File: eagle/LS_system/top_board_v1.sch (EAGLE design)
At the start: 18 parts, among them IC1 74HC595D, X1 MURDOCK_STACK

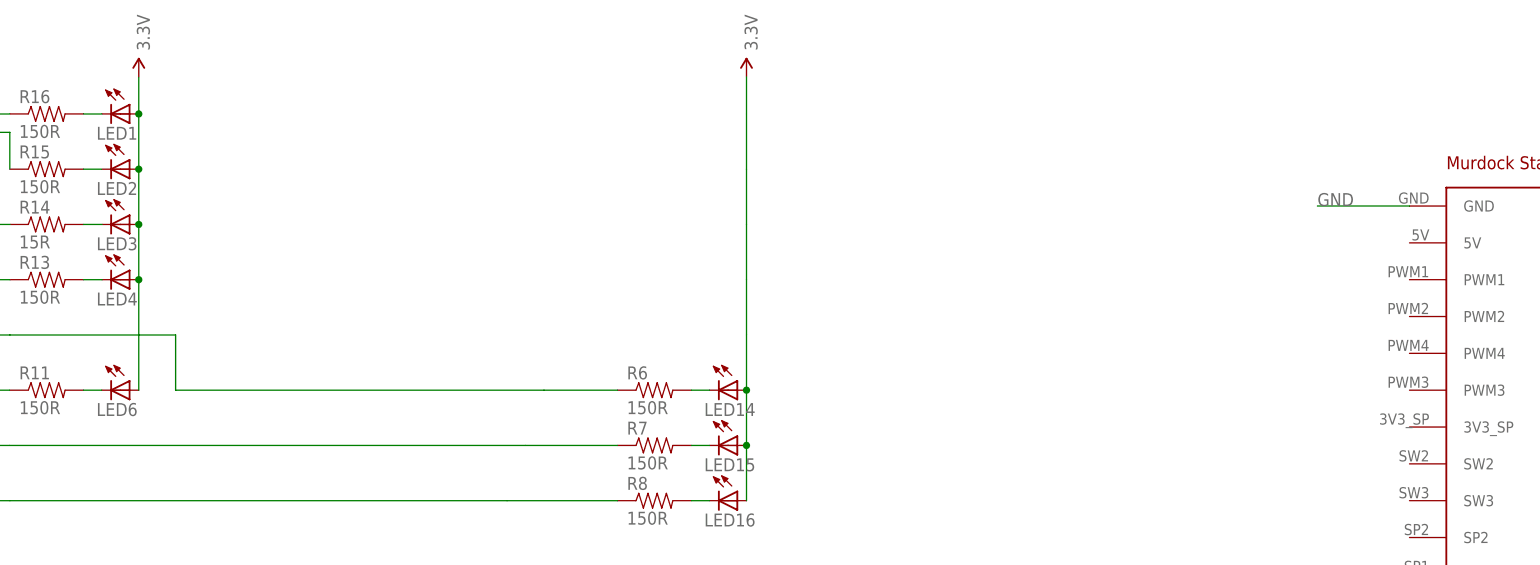
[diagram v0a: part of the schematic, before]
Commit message: conneced LEDs to switche 3v3
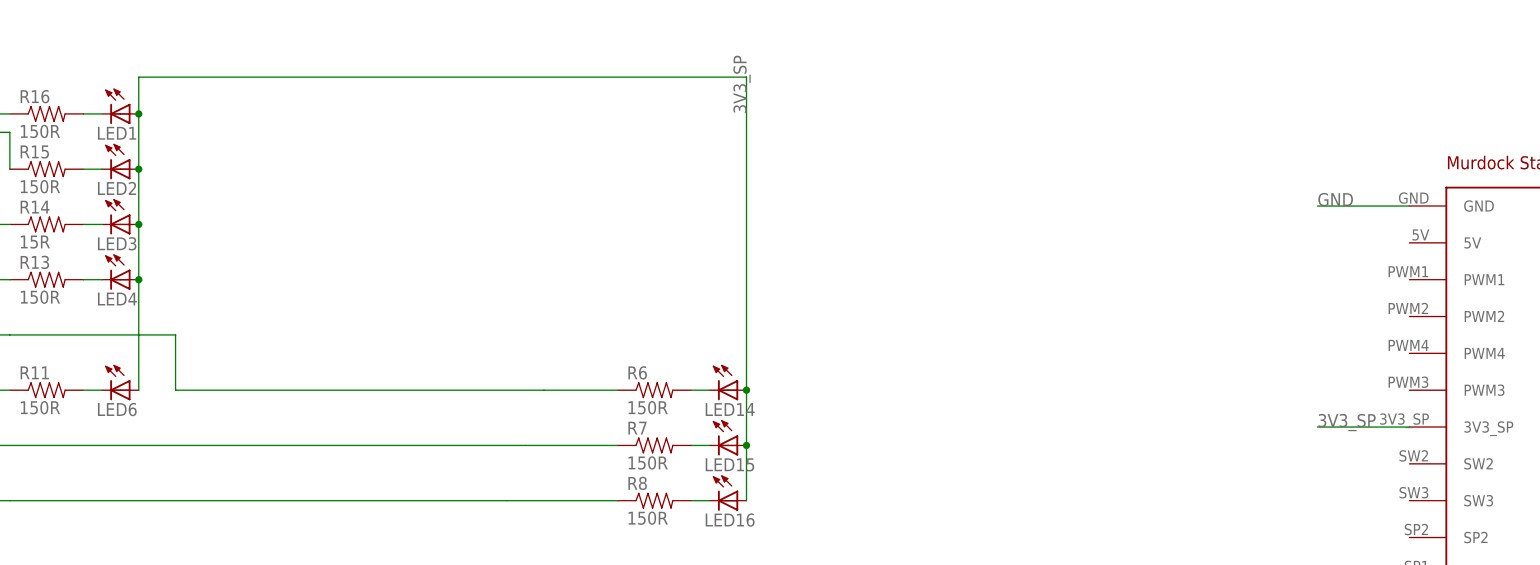
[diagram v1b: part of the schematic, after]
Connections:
- new net 3V3_SP: LED1.A, LED14.A, LED15.A, LED16.A, LED2.A, LED3.A, LED4.A, LED6.A, X1.3V3_SP
- net 3.3V: no longer LED1.A, LED14.A, LED15.A, LED16.A, LED2.A, LED3.A, LED4.A, LED6.A
